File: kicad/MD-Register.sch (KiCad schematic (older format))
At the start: 0 parts

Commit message: Finish todo list
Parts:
- added D? (x8): LED, symbol Device:LED
- added R? (x8): 220, symbol Device:R
- added U?: 74LS245, symbol 74xx:74LS245
- added U? (x2): 74LS173, symbol 74xx:74LS173
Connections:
- net BUS_0: now also U?.11 (B7), U?.11 (D3)
- net BUS_1: now also U?.12 (B6), U?.12 (D2)
- net BUS_2: now also U?.13 (B5), U?.13 (D1)
- net BUS_3: now also U?.14 (B4), U?.14 (D0)
- net BUS_4: now also U?.11 (D3), U?.15 (B3)
- net BUS_5: now also U?.12 (D2), U?.16 (B2)
- net BUS_6: now also U?.13 (D1), U?.17 (B1)
- net BUS_7: now also U?.14 (D0), U?.18 (B0)
- net RAM_0: now also D?.2 (A), U?.5 (A3), U?.6 (Q3)
- net RAM_1: now also D?.2 (A), U?.4 (A2), U?.5 (Q2)
- net RAM_2: now also D?.2 (A), U?.3 (A1), U?.4 (Q1)
- net RAM_3: now also D?.2 (A), U?.2 (A0), U?.3 (Q0)
- net RAM_4: now also D?.2 (A), U?.6 (Q3), U?.9 (A7)
- net RAM_5: now also D?.2 (A), U?.5 (Q2), U?.8 (A6)
- net RAM_6: now also D?.2 (A), U?.4 (Q1), U?.7 (A5)
- net RAM_7: now also D?.2 (A), U?.3 (Q0), U?.6 (A4)
- new net: D?.1 (K), R?.1 (x8)
- new net CLK: U?.7 (Cp), U?.7 (Cp)
- new net CLR: U?.15 (Mr), U?.15 (Mr)
- new net GND: R?.2, R?.2, R?.2, R?.2, R?.2, R?.2, R?.2, R?.2, U?.1 (Oe1), U?.1 (Oe1), U?.2 (Oe2), U?.2 (Oe2)
- new net VCC: U?.1 (A->B)
- new net ~MDI~: U?.10 (E2), U?.10 (E2), U?.9 (E1), U?.9 (E1)
- new net ~MDO~: U?.19 (CE)

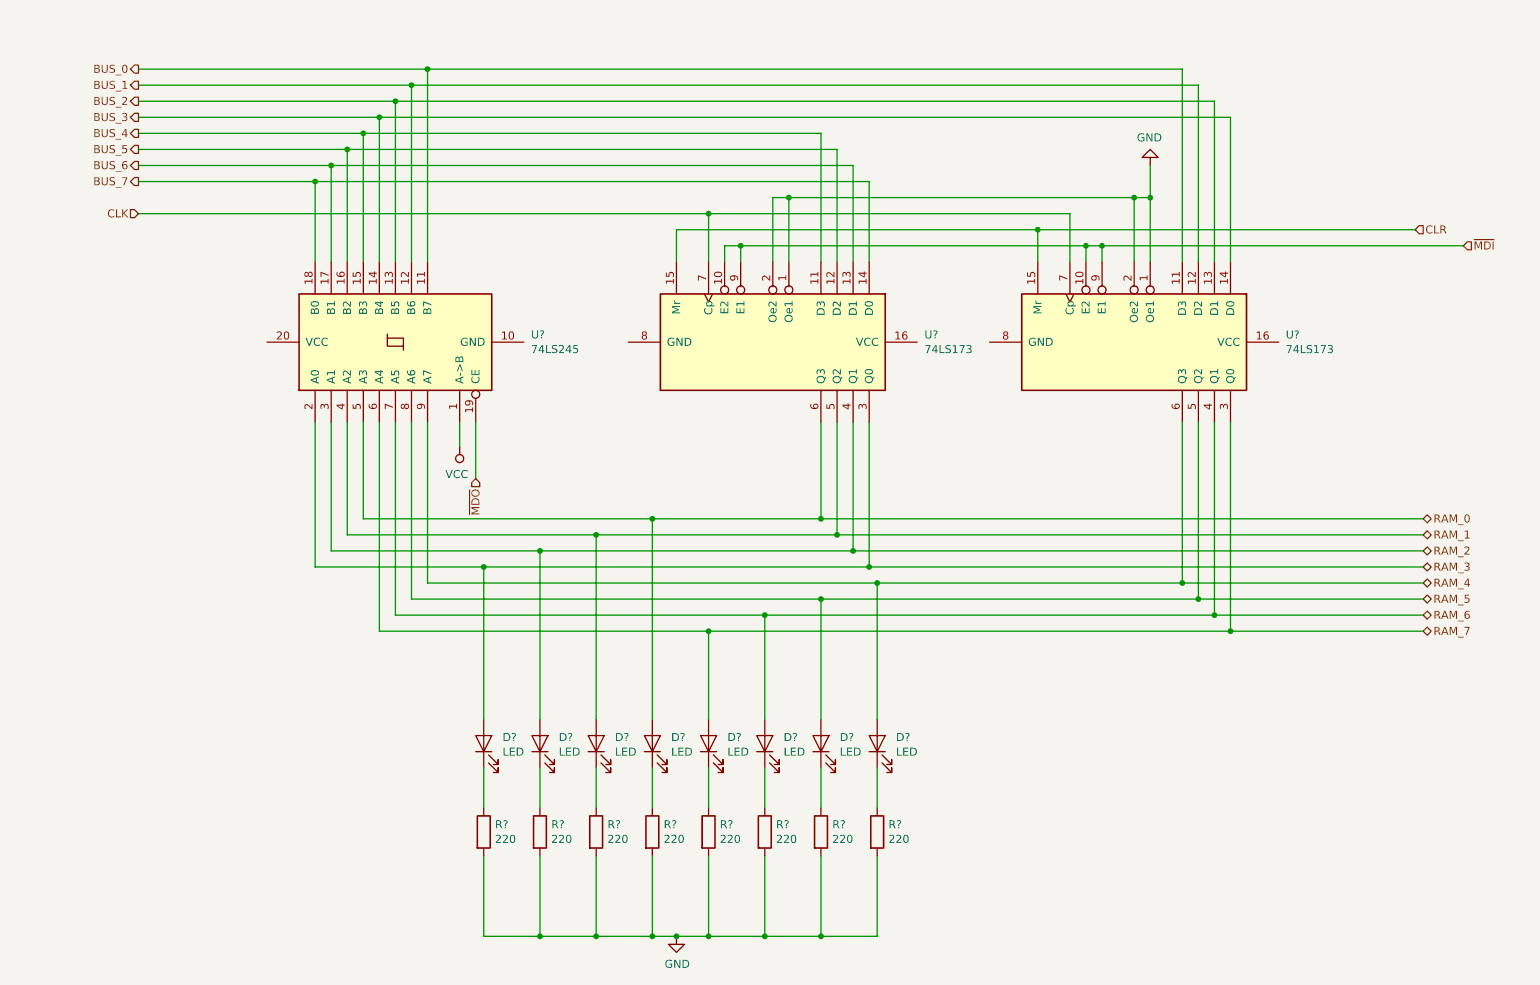
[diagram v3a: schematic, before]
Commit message: Reorganize part references
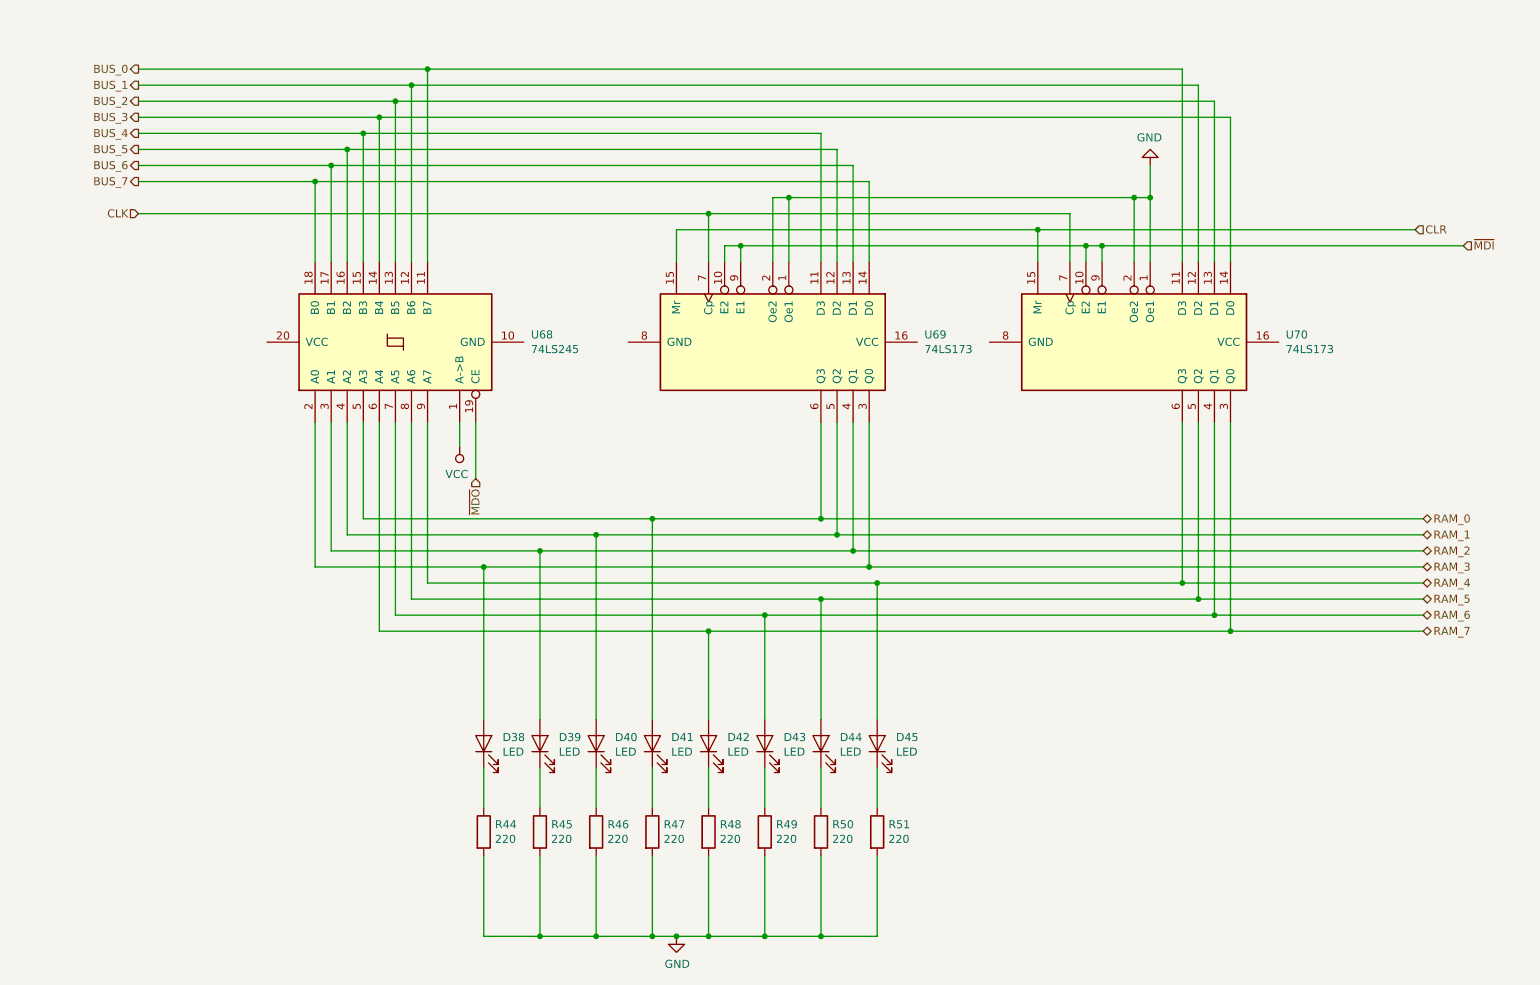
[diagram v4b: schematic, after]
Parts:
- gave numbers to parts that had none: 19
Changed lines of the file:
@@
 $Descr A4 11693 8268
 encoding utf-8
-Sheet 16 26
+Sheet 17 26
 Title ""
 Date "2019-10-03"
@@
 AR Path="/5DA98D6D/5DA9A5B3/5E61466D" Ref="U?"  Part="1"
 AR Path="/5DA9B7A7/5E61466D" Ref="U?"  Part="1"
-F 0 "U?" V 3196 2356 50  0000 R CNN
+AR Path="/5E5B2276/5D8079E9/5E61466D" Ref="U68"  Part="1"
+F 0 "U68" V 3196 2356 50  0000 R CNN
 F 1 "74LS245" V 3105 2356 50  0000 R CNN
 F 2 "" H 3150 3200 50  0001 C CNN
@@
 AR Path="/5DA98D6D/5DA9A5B3/5E61469A" Ref="U?"  Part="1"
 AR Path="/5DA9B7A7/5E61469A" Ref="U?"  Part="1"
-F 0 "U?" V 7704 4144 50  0000 L CNN
+AR Path="/5E5B2276/5D8079E9/5E61469A" Ref="U70"  Part="1"
+F 0 "U70" V 7704 4144 50  0000 L CNN
 F 1 "74LS173" V 7795 4144 50  0000 L CNN
 F 2 "" H 7750 3200 50  0001 C CNN
@@
 AR Path="/5DA98D6D/5DA9A5B3/5E6146C4" Ref="D?"  Part="1"
 AR Path="/5DA9B7A7/5E6146C4" Ref="D?"  Part="1"
-F 0 "D?" V 3739 5583 50  0000 R CNN
+AR Path="/5E5B2276/5D8079E9/5E6146C4" Ref="D38"  Part="1"
+F 0 "D38" V 3739 5583 50  0000 R CNN
 F 1 "LED" V 3648 5583 50  0000 R CNN
 F 2 "" H 3700 5700 50  0001 C CNN
@@
 AR Path="/5DA98D6D/5DA9A5B3/5E6146CA" Ref="D?"  Part="1"
 AR Path="/5DA9B7A7/5E6146CA" Ref="D?"  Part="1"
-F 0 "D?" V 4089 5583 50  0000 R CNN
+AR Path="/5E5B2276/5D8079E9/5E6146CA" Ref="D39"  Part="1"
+F 0 "D39" V 4089 5583 50  0000 R CNN
 F 1 "LED" V 3998 5583 50  0000 R CNN
 F 2 "" H 4050 5700 50  0001 C CNN
@@
 AR Path="/5DA98D6D/5DA9A5B3/5E6146D0" Ref="D?"  Part="1"
 AR Path="/5DA9B7A7/5E6146D0" Ref="D?"  Part="1"
-F 0 "D?" V 4439 5583 50  0000 R CNN
+AR Path="/5E5B2276/5D8079E9/5E6146D0" Ref="D40"  Part="1"
+F 0 "D40" V 4439 5583 50  0000 R CNN
 F 1 "LED" V 4348 5583 50  0000 R CNN
 F 2 "" H 4400 5700 50  0001 C CNN
@@
 AR Path="/5DA98D6D/5DA9A5B3/5E6146D6" Ref="D?"  Part="1"
 AR Path="/5DA9B7A7/5E6146D6" Ref="D?"  Part="1"
-F 0 "D?" V 4789 5583 50  0000 R CNN
+AR Path="/5E5B2276/5D8079E9/5E6146D6" Ref="D41"  Part="1"
+F 0 "D41" V 4789 5583 50  0000 R CNN
 F 1 "LED" V 4698 5583 50  0000 R CNN
 F 2 "" H 4750 5700 50  0001 C CNN
@@
 AR Path="/5DA98D6D/5DA9A5B3/5E6146DC" Ref="D?"  Part="1"
 AR Path="/5DA9B7A7/5E6146DC" Ref="D?"  Part="1"
-F 0 "D?" V 5139 5583 50  0000 R CNN
+AR Path="/5E5B2276/5D8079E9/5E6146DC" Ref="D42"  Part="1"
+F 0 "D42" V 5139 5583 50  0000 R CNN
 F 1 "LED" V 5048 5583 50  0000 R CNN
 F 2 "" H 5100 5700 50  0001 C CNN
@@
 AR Path="/5DA98D6D/5DA9A5B3/5E6146E2" Ref="D?"  Part="1"
 AR Path="/5DA9B7A7/5E6146E2" Ref="D?"  Part="1"
-F 0 "D?" V 5489 5583 50  0000 R CNN
+AR Path="/5E5B2276/5D8079E9/5E6146E2" Ref="D43"  Part="1"
+F 0 "D43" V 5489 5583 50  0000 R CNN
 F 1 "LED" V 5398 5583 50  0000 R CNN
 F 2 "" H 5450 5700 50  0001 C CNN
@@
 AR Path="/5DA98D6D/5DA9A5B3/5E6146E8" Ref="D?"  Part="1"
 AR Path="/5DA9B7A7/5E6146E8" Ref="D?"  Part="1"
-F 0 "D?" V 5839 5583 50  0000 R CNN
+AR Path="/5E5B2276/5D8079E9/5E6146E8" Ref="D44"  Part="1"
+F 0 "D44" V 5839 5583 50  0000 R CNN
 F 1 "LED" V 5748 5583 50  0000 R CNN
 F 2 "" H 5800 5700 50  0001 C CNN
@@
 AR Path="/5DA98D6D/5DA9A5B3/5E6146EE" Ref="D?"  Part="1"
 AR Path="/5DA9B7A7/5E6146EE" Ref="D?"  Part="1"
-F 0 "D?" V 6189 5583 50  0000 R CNN
+AR Path="/5E5B2276/5D8079E9/5E6146EE" Ref="D45"  Part="1"
+F 0 "D45" V 6189 5583 50  0000 R CNN
 F 1 "LED" V 6098 5583 50  0000 R CNN
 F 2 "" H 6150 5700 50  0001 C CNN
@@
 AR Path="/5DA98D6D/5DA9A5B3/5E61470A" Ref="R?"  Part="1"
 AR Path="/5DA9B7A7/5E61470A" Ref="R?"  Part="1"
-F 0 "R?" H 3770 6296 50  0000 L CNN
+AR Path="/5E5B2276/5D8079E9/5E61470A" Ref="R44"  Part="1"
+F 0 "R44" H 3770 6296 50  0000 L CNN
 F 1 "220" H 3770 6205 50  0000 L CNN
 F 2 "" V 3630 6250 50  0001 C CNN
@@
 AR Path="/5DA98D6D/5DA9A5B3/5E614710" Ref="R?"  Part="1"
 AR Path="/5DA9B7A7/5E614710" Ref="R?"  Part="1"
-F 0 "R?" H 4120 6296 50  0000 L CNN
+AR Path="/5E5B2276/5D8079E9/5E614710" Ref="R45"  Part="1"
+F 0 "R45" H 4120 6296 50  0000 L CNN
 F 1 "220" H 4120 6205 50  0000 L CNN
 F 2 "" V 3980 6250 50  0001 C CNN
@@
 AR Path="/5DA98D6D/5DA9A5B3/5E614716" Ref="R?"  Part="1"
 AR Path="/5DA9B7A7/5E614716" Ref="R?"  Part="1"
-F 0 "R?" H 4470 6296 50  0000 L CNN
+AR Path="/5E5B2276/5D8079E9/5E614716" Ref="R46"  Part="1"
+F 0 "R46" H 4470 6296 50  0000 L CNN
 F 1 "220" H 4470 6205 50  0000 L CNN
 F 2 "" V 4330 6250 50  0001 C CNN
@@
 AR Path="/5DA98D6D/5DA9A5B3/5E61471C" Ref="R?"  Part="1"
 AR Path="/5DA9B7A7/5E61471C" Ref="R?"  Part="1"
-F 0 "R?" H 4820 6296 50  0000 L CNN
+AR Path="/5E5B2276/5D8079E9/5E61471C" Ref="R47"  Part="1"
+F 0 "R47" H 4820 6296 50  0000 L CNN
 F 1 "220" H 4820 6205 50  0000 L CNN
 F 2 "" V 4680 6250 50  0001 C CNN
@@
 AR Path="/5DA98D6D/5DA9A5B3/5E614722" Ref="R?"  Part="1"
 AR Path="/5DA9B7A7/5E614722" Ref="R?"  Part="1"
-F 0 "R?" H 5170 6296 50  0000 L CNN
+AR Path="/5E5B2276/5D8079E9/5E614722" Ref="R48"  Part="1"
+F 0 "R48" H 5170 6296 50  0000 L CNN
 F 1 "220" H 5170 6205 50  0000 L CNN
 F 2 "" V 5030 6250 50  0001 C CNN
@@
 AR Path="/5DA98D6D/5DA9A5B3/5E614728" Ref="R?"  Part="1"
 AR Path="/5DA9B7A7/5E614728" Ref="R?"  Part="1"
-F 0 "R?" H 5520 6296 50  0000 L CNN
+AR Path="/5E5B2276/5D8079E9/5E614728" Ref="R49"  Part="1"
+F 0 "R49" H 5520 6296 50  0000 L CNN
 F 1 "220" H 5520 6205 50  0000 L CNN
 F 2 "" V 5380 6250 50  0001 C CNN
@@
 AR Path="/5DA98D6D/5DA9A5B3/5E61472E" Ref="R?"  Part="1"
 AR Path="/5DA9B7A7/5E61472E" Ref="R?"  Part="1"
-F 0 "R?" H 5870 6296 50  0000 L CNN
+AR Path="/5E5B2276/5D8079E9/5E61472E" Ref="R50"  Part="1"
+F 0 "R50" H 5870 6296 50  0000 L CNN
 F 1 "220" H 5870 6205 50  0000 L CNN
 F 2 "" V 5730 6250 50  0001 C CNN
@@
 AR Path="/5DA98D6D/5DA9A5B3/5E614734" Ref="R?"  Part="1"
 AR Path="/5DA9B7A7/5E614734" Ref="R?"  Part="1"
-F 0 "R?" H 6220 6296 50  0000 L CNN
+AR Path="/5E5B2276/5D8079E9/5E614734" Ref="R51"  Part="1"
+F 0 "R51" H 6220 6296 50  0000 L CNN
 F 1 "220" H 6220 6205 50  0000 L CNN
 F 2 "" V 6080 6250 50  0001 C CNN
@@
 AR Path="/5DA98D6D/5DA9A5B3/5E614742" Ref="#PWR?"  Part="1"
 AR Path="/5DA9B7A7/5E614742" Ref="#PWR?"  Part="1"
+AR Path="/5E5B2276/5D8079E9/5E614742" Ref="#PWR?"  Part="1"
 F 0 "#PWR?" H 4900 6650 50  0001 C CNN
 F 1 "GND" H 4905 6727 50  0000 C CNN
@@
 AR Path="/5DA98D6D/5DA9A5B3/5E61477E" Ref="#PWR?"  Part="1"
 AR Path="/5DA9B7A7/5E61477E" Ref="#PWR?"  Part="1"
+AR Path="/5E5B2276/5D8079E9/5E61477E" Ref="#PWR?"  Part="1"
 F 0 "#PWR?" H 3550 3700 50  0001 C CNN
 F 1 "VCC" H 3568 4023 50  0000 C CNN
@@
 AR Path="/5DA98D6D/5DA9A5B3/5E614785" Ref="U?"  Part="1"
 AR Path="/5DA9B7A7/5E614785" Ref="U?"  Part="1"
-F 0 "U?" V 5454 4144 50  0000 L CNN
+AR Path="/5E5B2276/5D8079E9/5E614785" Ref="U69"  Part="1"
+F 0 "U69" V 5454 4144 50  0000 L CNN
 F 1 "74LS173" V 5545 4144 50  0000 L CNN
 F 2 "" H 5500 3200 50  0001 C CNN
@@
 AR Path="/5DA98D6D/5DA9A5B3/5E61479D" Ref="#PWR?"  Part="1"
 AR Path="/5DA9B7A7/5E61479D" Ref="#PWR?"  Part="1"
+AR Path="/5E5B2276/5D8079E9/5E61479D" Ref="#PWR?"  Part="1"
 F 0 "#PWR?" H 7850 1850 50  0001 C CNN
 F 1 "GND" H 7855 1927 50  0000 C CNN

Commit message: Up to v1.0 and plot
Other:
- moved on the sheet: D38, D39, D40, D41, D42, D43, D44, D45, R44, R45, R46, R47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
